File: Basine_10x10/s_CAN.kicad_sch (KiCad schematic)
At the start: 15 parts, among them U1 SRV05-4, U4 SN65HVD230

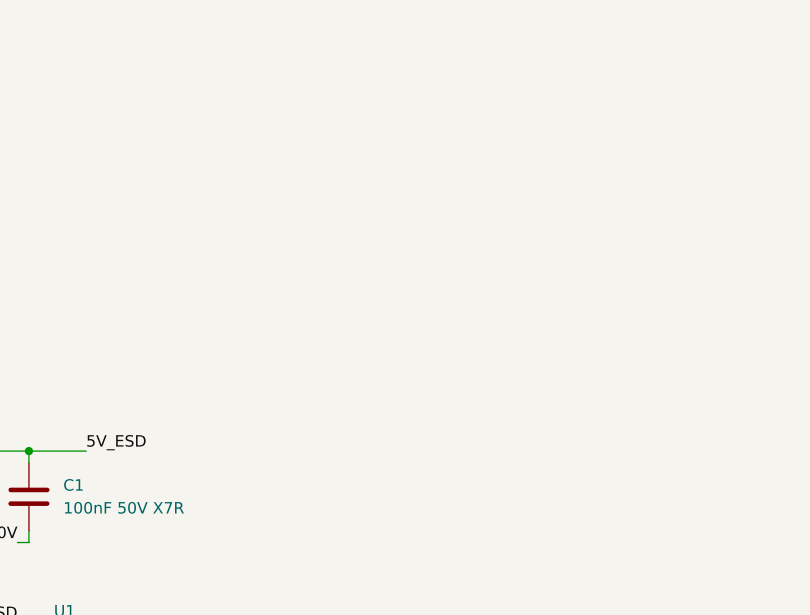
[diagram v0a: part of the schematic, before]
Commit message: 10x10
placement et routage du CAN
divers
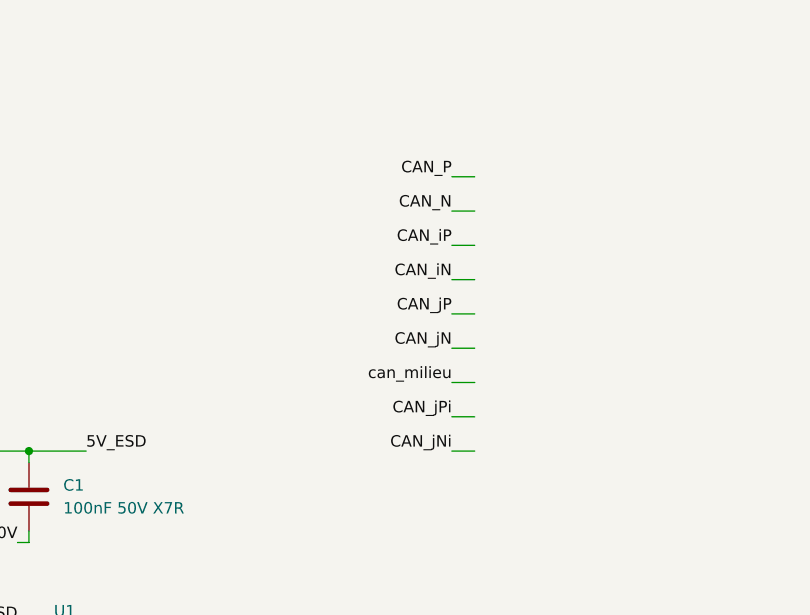
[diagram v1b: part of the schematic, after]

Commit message: passage au pas de 2,54mm pour toutes les allumettes
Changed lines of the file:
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@@
 (kicad_sch
-	(version 20231120)
+	(version 20250114)
 	(generator "eeschema")
-	(generator_version "8.0")
+	(generator_version "9.0")
 	(paper "A4")
 	(title_block
@@
 		(rev "0")
 	)
+	(text "ACT45B-510-2P-TL003\nC76584\n\nou\nCUW43T-513T-AU\nC2847109\n"
+		(exclude_from_sim no)
+		(at 78.232 116.078 0)
+		(effects
+			(font
+				(size 1.27 1.27)
+			)
+			(justify left bottom)
+		)
+	)
 	(junction
 		(at 168.91 99.06)
@@
 		)
 	)
-	(text "ACT45B-510-2P-TL003\nC76584\n\nou\nCUW43T-513T-AU\nC2847109\n"
-		(exclude_from_sim no)
-		(at 78.232 116.078 0)
-		(effects
-			(font
-				(size 1.27 1.27)
-			)
-			(justify left bottom)
-		)
-	)
 	(label "3V3"
 		(at 242.57 91.44 180)
-		(fields_autoplaced yes)
 		(effects
 			(font
@@
 	(label "3V3"
 		(at 35.56 22.86 0)
-		(fields_autoplaced yes)
 		(effects
 			(font
@@
 	(label "CAN_N"
 		(at 80.01 96.52 180)
-		(fields_autoplaced yes)
 		(effects
 			(font
@@
 	(label "CAN_RX"
 		(at 231.14 100.33 180)
-		(fields_autoplaced yes)
 		(effects
 			(font
@@
 	(label "CAN_iP"
 		(at 256.54 100.33 0)
-		(fields_autoplaced yes)
 		(effects
 			(font
@@
 	(label "0V"
 		(at 242.57 85.09 180)
-		(fields_autoplaced yes)
 		(effects
 			(font
@@
 	(label "0V"
 		(at 242.57 111.76 180)
-		(fields_autoplaced yes)
 		(effects
 			(font
@@
 	(label "CAN_TX"
 		(at 231.14 97.79 180)
-		(fields_autoplaced yes)
 		(effects
 			(font
@@
 	(label "5V"
 		(at 31.75 64.77 180)
-		(fields_autoplaced yes)
 		(effects
 			(font
@@
 	(label "3V3"
 		(at 242.57 77.47 180)
-		(fields_autoplaced yes)
 		(effects
 			(font
@@
 	(label "CAN_jNi"
 		(at 93.98 64.77 180)
-		(fields_autoplaced yes)
 		(effects
 			(font
@@
 	(label "CAN_P"
 		(at 35.56 30.48 0)
-		(fields_autoplaced yes)
 		(effects
 			(font
@@
 	(label "CAN_P"
 		(at 31.75 95.25 180)
-		(fields_autoplaced yes)
 		(effects
 			(font
@@
 	(label "CAN_RX"
 		(at 34.29 41.91 0)
-		(fields_autoplaced yes)
 		(effects
 			(font
@@
 	(label "CAN_jPi"
 		(at 152.4 99.06 0)
-		(fields_autoplaced yes)
 		(effects
 			(font
@@
 	(label "5V"
 		(at 35.56 19.05 0)
-		(fields_autoplaced yes)
 		(effects
 			(font
@@
 	(label "CAN_P"
 		(at 62.23 100.33 0)
-		(fields_autoplaced yes)
 		(effects
 			(font
@@
 	(label "5V_ESD"
 		(at 53.34 64.77 0)
-		(fields_autoplaced yes)
 		(effects
 			(font
@@
 	(label "CAN_jP"
 		(at 132.08 96.52 0)
-		(fields_autoplaced yes)
 		(effects
 			(font
@@
 	(label "CAN_iN"
 		(at 256.54 102.87 0)
-		(fields_autoplaced yes)
 		(effects
 			(font
@@
 	(label "can_milieu"
 		(at 93.98 57.15 180)
-		(fields_autoplaced yes)
 		(effects
 			(font
@@
 	(label "0V"
 		(at 35.56 26.67 0)
-		(fields_autoplaced yes)
 		(effects
 			(font
@@
 	(label "CAN_N"
 		(at 35.56 33.02 0)
-		(fields_autoplaced yes)
 		(effects
 			(font
@@
 	(label "CAN_TX"
 		(at 34.29 39.37 0)
-		(fields_autoplaced yes)
 		(effects
 			(font
@@
 	(label "CAN_iN"
 		(at 116.84 102.87 180)
-		(fields_autoplaced yes)
 		(effects
 			(font
@@
 	(label "Vref_can"
 		(at 231.14 102.87 180)
-		(fields_autoplaced yes)
 		(effects
 			(font
@@
 	(label "CAN_jN"
 		(at 93.98 53.34 180)
-		(fields_autoplaced yes)
 		(effects
 			(font
@@
 	(label "CAN_jNi"
 		(at 152.4 105.41 0)
-		(fields_autoplaced yes)
 		(effects
 			(font
@@
 	(label "0V"
 		(at 45.72 74.93 180)
-		(fields_autoplaced yes)
 		(effects
 			(font
@@
 	(label "CAN_iN"
 		(at 97.79 96.52 0)
-		(fields_autoplaced yes)
 		(effects
 			(font
@@
 	(label "CAN_iP"
 		(at 97.79 99.06 0)
-		(fields_autoplaced yes)
 		(effects
 			(font
@@
 	(label "can_milieu"
 		(at 168.91 99.06 0)
-		(fields_autoplaced yes)
 		(effects
 			(font
@@
 	(label "0V"
 		(at 45.72 111.76 180)
-		(fields_autoplaced yes)
 		(effects
 			(font
@@
 	(label "5V_ESD"
 		(at 45.72 83.82 180)
-		(fields_autoplaced yes)
 		(effects
 			(font
@@
 	(label "CAN_jPi"
 		(at 93.98 60.96 180)
-		(fields_autoplaced yes)
 		(effects
 			(font
@@
 	(label "0V"
 		(at 172.72 109.22 180)
-		(fields_autoplaced yes)
 		(effects
 			(font
@@
 	(label "CAN_P"
 		(at 93.98 34.29 180)
-		(fields_autoplaced yes)
 		(effects
 			(font
@@
 	(label "CAN_iP"
 		(at 93.98 41.91 180)
-		(fields_autoplaced yes)
 		(effects
 			(font
@@
 	(label "Vref_can"
 		(at 193.04 99.06 0)
-		(fields_autoplaced yes)
 		(effects
 			(font
@@
 	(label "CAN_iN"
 		(at 93.98 45.72 180)
-		(fields_autoplaced yes)
 		(effects
 			(font
@@
 	(label "CAN_N"
 		(at 93.98 38.1 180)
-		(fields_autoplaced yes)
 		(effects
 			(font
@@
 	(label "CAN_N"
 		(at 62.23 95.25 0)
-		(fields_autoplaced yes)
 		(effects
 			(font
@@
 	(label "CAN_N"
 		(at 31.75 100.33 180)
-		(fields_autoplaced yes)
 		(effects
 			(font
@@
 	(label "0V"
 		(at 220.98 105.41 180)
-		(fields_autoplaced yes)
 		(effects
 			(font
@@
 	(label "CAN_iP"
 		(at 116.84 96.52 180)
-		(fields_autoplaced yes)
 		(effects
 			(font
@@
 	(label "CAN_jN"
 		(at 132.08 102.87 0)
-		(fields_autoplaced yes)
 		(effects
 			(font
@@
 	(label "CAN_P"
 		(at 80.01 99.06 180)
-		(fields_autoplaced yes)
 		(effects
 			(font
@@
 	(label "CAN_jP"
 		(at 93.98 49.53 180)
-		(fields_autoplaced yes)
 		(effects
 			(font
@@
 		(shape input)
 		(at 33.02 33.02 180)
-		(fields_autoplaced yes)
 		(effects
 			(font
@@
 		(shape input)
 		(at 31.75 41.91 180)
-		(fields_autoplaced yes)
 		(effects
 			(font
@@
 		(shape input)
 		(at 31.75 39.37 180)
-		(fields_autoplaced yes)
 		(effects
 			(font
@@
 		(shape input)
 		(at 33.02 26.67 180)
-		(fields_autoplaced yes)
 		(effects
 			(font
@@
 		(shape input)
 		(at 33.02 19.05 180)
-		(fields_autoplaced yes)
 		(effects
 			(font
@@
 		(shape input)
 		(at 33.02 22.86 180)
-		(fields_autoplaced yes)
 		(effects
 			(font
@@
 		(shape input)
 		(at 33.02 30.48 180)
-		(fields_autoplaced yes)
-		(effects
-			(font
+		(effects
+			(font
